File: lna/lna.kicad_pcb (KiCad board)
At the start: 2 copper layers, 40 x 20 mm, 1 part, among them U1 PGA-103+

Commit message: PCB part 1
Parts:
- added C1: 47pF, Capacitor_SMD:C_0603_1608Metric, F.Cu at (138.4, 103.0)
- added C2: 1.2pF, Capacitor_SMD:C_0603_1608Metric, F.Cu at (134.5, 95.0)
- added C3: 330pF, Capacitor_SMD:C_0603_1608Metric, F.Cu at (155.0, 99.0)
- added C4: 0.33uF, Capacitor_SMD:C_0603_1608Metric, F.Cu at (153.0, 89.5)
- added C5: 10uF, Capacitor_Tantalum_SMD:CP_EIA-3216-18_Kemet-A, F.Cu at (153.0, 87.0)
- added C6: 0.01uF, Capacitor_SMD:C_0603_1608Metric, F.Cu at (153.0, 95.0)
- added J1: Conn_Coaxial, Connector_Coaxial:SMA_Amphenol_132289_EdgeMount, F.Cu at (128.0, 95.0)
- added J2: V5-GND, Connector_PinHeader_2.54mm:PinHeader_1x02_P2.54mm_Vertical, F.Cu at (143.5, 87.0)
- added J3: Conn_Coaxial, Connector_Coaxial:SMA_Amphenol_132289_EdgeMount, F.Cu at (162.0, 95.0)
- added L1: 3nH, Inductor_SMD:L_0805_2012Metric, F.Cu at (138.4, 99.0)
- added L2: 120nH, Inductor_SMD:L_0805_2012Metric, F.Cu at (138.4, 95.0)
- added L3: 310nH, Inductor_SMD:L_0805_2012Metric, F.Cu at (142.9, 99.0)
- added L4: 310nH, Inductor_SMD:L_0805_2012Metric, F.Cu at (147.0, 99.0)
- added L5: 220nH, Inductor_SMD:L_0805_2012Metric, F.Cu at (153.0, 92.0)
- added R1: 150R, Resistor_SMD:R_0603_1608Metric, F.Cu at (151.0, 99.0)
- moved U1 1.70 mm to (145.0, 93.3), turned to 90 degrees
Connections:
- U1 pad 1: (no net) -> Net-(L2-Pad2)
- U1 pad 2: (no net) -> GND
- U1 pad 3: (no net) -> Net-(C6-Pad1)

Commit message: Routes
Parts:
- moved L2 0.06 mm to (138.5, 95.0), turned to 180 degrees
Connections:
- L2 pad 1: Net-(C2-Pad2) -> Net-(L3-Pad1)
- L2 pad 2: Net-(L2-Pad2) -> Net-(C2-Pad2)
- L3 pad 1: Net-(L2-Pad2) -> Net-(L3-Pad1)
- U1 pad 1: Net-(L2-Pad2) -> Net-(L3-Pad1)
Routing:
- net GND: track 0.00 -> 85.4 mm, vias 0 -> 4
- net Net-(C1-Pad1): track 0.00 -> 16.8 mm
- net 5V: track 0.00 -> 10.9 mm
- net Net-(C6-Pad1): track 0.00 -> 7.15 mm
- net Net-(C6-Pad2): track 0.00 -> 7.11 mm
- net Net-(L3-Pad1): track 0.00 -> 6.29 mm
- net Net-(C3-Pad1): track 0.00 -> 2.43 mm
- net Net-(L4-Pad2): track 0.00 -> 2.28 mm
- net Net-(L3-Pad2): track 0.00 -> 2.19 mm
- added copper zone on F.Cu, net GND
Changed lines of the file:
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@@
   (net 6 "Net-(C6-Pad2)")
   (net 7 "Net-(C6-Pad1)")
-  (net 8 "Net-(L2-Pad2)")
+  (net 8 "Net-(L3-Pad1)")
   (net 9 "Net-(L3-Pad2)")
   (net 10 "Net-(L4-Pad2)")
@@
     (fp_line (start 1.55 -2.25) (end 1.55 2.25) (layer "F.Fab") (width 0.1))
     (pad "1" smd rect (at -1.65 -1.5 90) (size 1.3 0.9) (layers "F.Cu" "F.Paste" "F.Mask")
-      (net 8 "Net-(L2-Pad2)"))
+      (net 8 "Net-(L3-Pad1)"))
     (pad "2" smd custom (at -1.5625 0 90) (size 1.475 0.9) (layers "F.Cu" "F.Paste" "F.Mask")
       (net 1 "GND") (pinfunction "GND") (zone_connect 2)
@@
   )
   (footprint "Inductor_SMD:L_0805_2012Metric" (layer "F.Cu")
-    (at 138.4375 95)
+    (at 138.5 95 180)
     (descr "Inductor SMD 0805 (2012 Metric), square (rectangular) end terminal, IPC_7351 nominal, (Body size source: https://docs.google.com/spreadsheets/d/1BsfQQcO9C6DZCsRaXUlFlo91Tg2WpOkGARC1WS5S8t0/edit?usp=sharing), generated with kicad-footprint-generator")
     (tags "inductor")
@@
     (property "Sheet name" "")
     (attr smd)
-    (fp_text reference "L2" (at 0 -1.65) (layer "F.SilkS")
+    (fp_text reference "L2" (at 0 1.5) (layer "F.SilkS")
       (effects (font (size 0.75 0.75) (thickness 0.15)))
     )
@@
     (fp_line (start 1 -0.6) (end 1 0.6) (layer "F.Fab") (width 0.1))
     (fp_line (start 1 0.6) (end -1 0.6) (layer "F.Fab") (width 0.1))
-    (pad "1" smd roundrect (at -0.9375 0) (size 0.975 1.4) (layers "F.Cu" "F.Paste" "F.Mask") (roundrect_rratio 0.25)
-      (net 3 "Net-(C2-Pad2)") (pinfunction "1"))
-    (pad "2" smd roundrect (at 0.9375 0) (size 0.975 1.4) (layers "F.Cu" "F.Paste" "F.Mask") (roundrect_rratio 0.25)
-      (net 8 "Net-(L2-Pad2)") (pinfunction "2"))
+    (pad "1" smd roundrect (at -0.9375 0 180) (size 0.975 1.4) (layers "F.Cu" "F.Paste" "F.Mask") (roundrect_rratio 0.25)
+      (net 8 "Net-(L3-Pad1)") (pinfunction "1"))
+    (pad "2" smd roundrect (at 0.9375 0 180) (size 0.975 1.4) (layers "F.Cu" "F.Paste" "F.Mask") (roundrect_rratio 0.25)
+      (net 3 "Net-(C2-Pad2)") (pinfunction "2"))
     (model "${KISYS3DMOD}/Inductor_SMD.3dshapes/L_0805_2012Metric.wrl"
       (offset (xyz 0 0 0))
@@
     (fp_line (start 1 0.6) (end -1 0.6) (layer "F.Fab") (width 0.1))
     (pad "1" smd roundrect (at -0.9375 0) (size 0.975 1.4) (layers "F.Cu" "F.Paste" "F.Mask") (roundrect_rratio 0.25)
-      (net 8 "Net-(L2-Pad2)") (pinfunction "1"))
+      (net 8 "Net-(L3-Pad1)") (pinfunction "1"))
     (pad "2" smd roundrect (at 0.9375 0) (size 0.975 1.4) (layers "F.Cu" "F.Paste" "F.Mask") (roundrect_rratio 0.25)
       (net 9 "Net-(L3-Pad2)") (pinfunction "2"))
@@
     (style (thickness 0.15) (arrow_length 1.27) (text_position_mode 0) (extension_height 0.58642) (extension_offset 0.5) keep_text_aligned)
   )
+  (segment (start 145 91.5) (end 145 94.8625) (width 1) (layer "F.Cu") (net 1))
+  (segment (start 162 99.25) (end 156.0375 99.25) (width 1) (layer "F.Cu") (net 1))
+  (segment (start 153.7875 89.5) (end 153.7875 87.5625) (width 1) (layer "F.Cu") (net 1))
+  (segment (start 162 90.75) (end 158.25 87) (width 1) (layer "F.Cu") (net 1))
+  (segment (start 156.0375 99.25) (end 155.7875 99) (width 1) (layer "F.Cu") (net 1))
+  (segment (start 128 90.75) (end 128 88.5) (width 1) (layer "F.Cu") (net 1))
+  (segment (start 162 90.75) (end 162 88.5) (width 1) (layer "F.Cu") (net 1))
+  (segment (start 143.5 90) (end 145 91.5) (width 1) (layer "F.Cu") (net 1))
+  (segment (start 139.375 99) (end 139.375 102.85) (width 1) (layer "F.Cu") (net 1))
+  (segment (start 143.5 87) (end 143.5 90) (width 1) (layer "F.Cu") (net 1))
+  (segment (start 128 101.5) (end 128 99.25) (width 1) (layer "F.Cu") (net 1))
+  (segment (start 153.7875 87.5625) (end 154.35 87) (width 1) (layer "F.Cu") (net 1))
+  (segment (start 162 99.25) (end 162 101.5) (width 1) (layer "F.Cu") (net 1))
+  (segment (start 158.25 87) (end 154.35 87) (width 1) (layer "F.Cu") (net 1))
+  (segment (start 139.375 102.85) (end 139.225 103) (width 1) (layer "F.Cu") (net 1))
+  (segment (start 162 101.5) (end 162 98) (width 1) (layer "F.Cu") (net 1))
+  (via (at 162 88.5) (size 0.8) (drill 0.4) (layers "F.Cu" "B.Cu") (net 1))
+  (via (at 128 101.5) (size 0.8) (drill 0.4) (layers "F.Cu" "B.Cu") (net 1))
+  (via (at 128 88.5) (size 0.8) (drill 0.4) (layers "F.Cu" "B.Cu") (net 1))
+  (via (at 162 101.5) (size 0.8) (drill 0.4) (layers "F.Cu" "B.Cu") (net 1))
+  (segment (start 128 88.5) (end 129.5 87) (width 1) (layer "B.Cu") (net 1))
+  (segment (start 128 101.5) (end 128 99.25) (width 1) (layer "B.Cu") (net 1))
+  (segment (start 162 99.25) (end 162 90.75) (width 1) (layer "B.Cu") (net 1))
+  (segment (start 162 90.75) (end 162 88.5) (width 1) (layer "B.Cu") (net 1))
+  (segment (start 128 90.75) (end 128 88.5) (width 1) (layer "B.Cu") (net 1))
+  (segment (start 131.75 87) (end 143.5 87) (width 1) (layer "B.Cu") (net 1))
+  (segment (start 128 99.25) (end 128 90.75) (width 1) (layer "B.Cu") (net 1))
+  (segment (start 129.5 87) (end 131.75 87) (width 1) (layer "B.Cu") (net 1))
+  (segment (start 162 99.25) (end 162 101.5) (width 1) (layer "B.Cu") (net 1))
+  (segment (start 133 95) (end 128 95) (width 3) (layer "F.Cu") (net 2))
+  (segment (start 133.75 95) (end 133.75 97.75) (width 1) (layer "F.Cu") (net 2))
+  (segment (start 137.65 99.15) (end 137.5 99) (width 1) (layer "F.Cu") (net 2))
+  (segment (start 137.65 103) (end 137.65 99.15) (width 1) (layer "F.Cu") (net 2))
+  (segment (start 135 99) (end 137.5 99) (width 1) (layer "F.Cu") (net 2))
+  (segment (start 133.75 97.75) (end 135 99) (width 1) (layer "F.Cu") (net 2))
+  (segment (start 133.75 95) (end 133 95) (width 1) (layer "F.Cu") (net 2))
+  (segment (start 136.325 95) (end 136.8 95) (width 3) (layer "F.Cu") (net 3))
+  (segment (start 154.2125 99) (end 151.7875 99) (width 1) (layer "F.Cu") (net 4))
+  (segment (start 151.65 88.9375) (end 152.2125 89.5) (width 1) (layer "F.Cu") (net 5))
+  (segment (start 152.2125 91.85) (end 152.0625 92) (width 1) (layer "F.Cu") (net 5))
+  (segment (start 151.65 87) (end 151.65 88.9375) (width 1) (layer "F.Cu") (net 5))
+  (segment (start 146.04 87) (end 151.65 87) (width 1) (layer "F.Cu") (net 5))
+  (segment (start 152.2125 89.5) (end 152.2125 91.85) (width 1) (layer "F.Cu") (net 5))
+  (segment (start 154.8875 95) (end 162 95) (width 3) (layer "F.Cu") (net 6))
+  (segment (start 152.1625 94.95) (end 152.2125 95) (width 1) (layer "F.Cu") (net 7))
+  (segment (start 147.8 94.95) (end 151.1625 94.95) (width 3) (layer "F.Cu") (net 7))
+  (segment (start 153.9375 92) (end 153.9375 92.7) (width 1) (layer "F.Cu") (net 7))
+  (segment (start 152.2125 94.425) (end 153.9375 92.7) (width 1) (layer "F.Cu") (net 7))
+  (segment (start 152.2125 94.425) (end 152.2125 95) (width 1) (layer "F.Cu") (net 7))
+  (segment (start 141.5 95) (end 141.5 97.5) (width 1) (layer "F.Cu") (net 8))
+  (segment (start 141.5 98.5) (end 142 99) (width 1) (layer "F.Cu") (net 8))
+  (segment (start 141.5 97.5) (end 141.5 98.5) (width 1) (layer "F.Cu") (net 8))
+  (segment (start 143.45 95) (end 143.5 94.95) (width 1) (layer "F.Cu") (net 8))
+  (segment (start 140.4375 95) (end 142.45 95) (width 3) (layer "F.Cu") (net 8))
+  (segment (start 146.0625 99) (end 143.875 99) (width 1) (layer "F.Cu") (net 9))
+  (segment (start 150.2125 99) (end 147.9375 99) (width 1) (layer "F.Cu") (net 10))
+  (zone (net 1) (net_name "GND") (layer "F.Cu") (hatch edge 0.508)
+    (connect_pads (clearance 0.508))
+    (min_thickness 0.254) (filled_areas_thickness no)
+    (fill yes (thermal_gap 0.508) (thermal_bridge_width 0.508))
+    (polygon
+      (pts
+        (xy 165 105)
+        (xy 125 105)
+        (xy 125 85)
+        (xy 165 85)
+      )
+    )
+  )
 )

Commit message: Final v1
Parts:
- added FB1: 600R/0.5A, fbead:Murata-BLM18-0.15-t0.8-0-0-IPC_A, F.Cu at (150.0, 87.8)
- moved C3 5.94 mm to (149.2, 100.2)
- moved C1 5.60 mm to (133.6, 100.2)
- moved R1 5.34 mm to (145.8, 100.2)
- moved L1 4.97 mm to (133.6, 97.9)
- moved L4 4.95 mm to (142.2, 100.2)
- moved L3 2.37 mm to (141.4, 97.2), turned to -90 degrees
- moved C5 1.79 mm to (154.6, 87.8)
- moved C4 1.12 mm to (154.0, 90.0)
- moved L5 0.76 mm to (152.3, 92.2), turned to 0 degrees
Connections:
- C4 pad 1: 5V -> Net-(C4-Pad1)
- C5 pad 1: 5V -> Net-(C4-Pad1)
- L5 pad 2: 5V -> Net-(C4-Pad1)
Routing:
- net GND: track 85.4 -> 33.8 mm, vias 4 -> 6
- net 5V: track 10.9 -> 3.52 mm
- net Net-(C4-Pad1): track 0.00 -> 6.89 mm
- net Net-(C1-Pad1): track 16.8 -> 11.2 mm
- net Net-(L2-Pad1): track 6.29 -> 2.08 mm
- net Net-(C3-Pad1): track 2.43 -> 1.81 mm
- added copper zone on B.Cu, net GND

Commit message: Add some fixes
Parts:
- added C7: 100pF, Capacitor_SMD:C_0603_1608Metric, F.Cu at (153.0, 95.0)
- added G***: LOGO, lna_images:name, F.Cu at (130.8, 103.8)
- C4: value 0.33uF -> 100pF
- C5: value 10uF -> 100nF; footprint Capacitor_Tantalum_SMD:CP_EIA-3216-18_Kemet-A -> Capacitor_SMD:C_0603_1608Metric
- C6: value 0.01uF -> 10uF; footprint Capacitor_SMD:C_0603_1608Metric -> Capacitor_Tantalum_SMD:CP_EIA-3216-18_Kemet-A
- moved C6 8.66 mm to (155.8, 86.8)
- moved C1 7.66 mm to (132.6, 92.6), turned to 90 degrees
- moved C5 1.20 mm to (154.7, 89.0)
- moved L5 1.06 mm to (151.2, 92.2)
- moved C4 1.05 mm to (154.7, 90.8), turned to 180 degrees
- moved L1 1.04 mm to (132.6, 97.6), turned to -90 degrees
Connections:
- C4 pad 1: Net-(C4-Pad1) -> GND
- C4 pad 2: GND -> Net-(C4-Pad2)
- C5 pad 1: Net-(C4-Pad1) -> Net-(C4-Pad2)
- C6 pad 1: Net-(C6-Pad1) -> Net-(C4-Pad2)
- C6 pad 2: Net-(C6-Pad2) -> GND
- FB1 pad 2: Net-(C4-Pad1) -> Net-(C4-Pad2)
- J3 pad 1: Net-(C6-Pad2) -> Net-(C7-Pad2)
- L5 pad 1: Net-(C6-Pad1) -> Net-(C7-Pad1)
- L5 pad 2: Net-(C4-Pad1) -> Net-(C4-Pad2)
- U1 pad 3: Net-(C6-Pad1) -> Net-(C7-Pad1)
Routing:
- net Net-(C4-Pad2): track 0.00 -> 9.92 mm
- net Net-(C7-Pad1): track 0.00 -> 7.91 mm
- net Net-(C6-Pad1): track 7.54 -> 0.00 mm
- net Net-(C7-Pad2): track 0.00 -> 7.11 mm
- net Net-(C6-Pad2): track 7.11 -> 0.00 mm
- net Net-(C4-Pad1): track 6.89 -> 0.00 mm
- net Net-(C1-Pad1): track 11.2 -> 6.24 mm
- net GND: track 33.8 -> 32.7 mm, vias 6 -> 7

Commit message: Refill zones
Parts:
- moved G*** 3.26 mm to (134.0, 103.2)
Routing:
- net GND: vias 7 -> 8

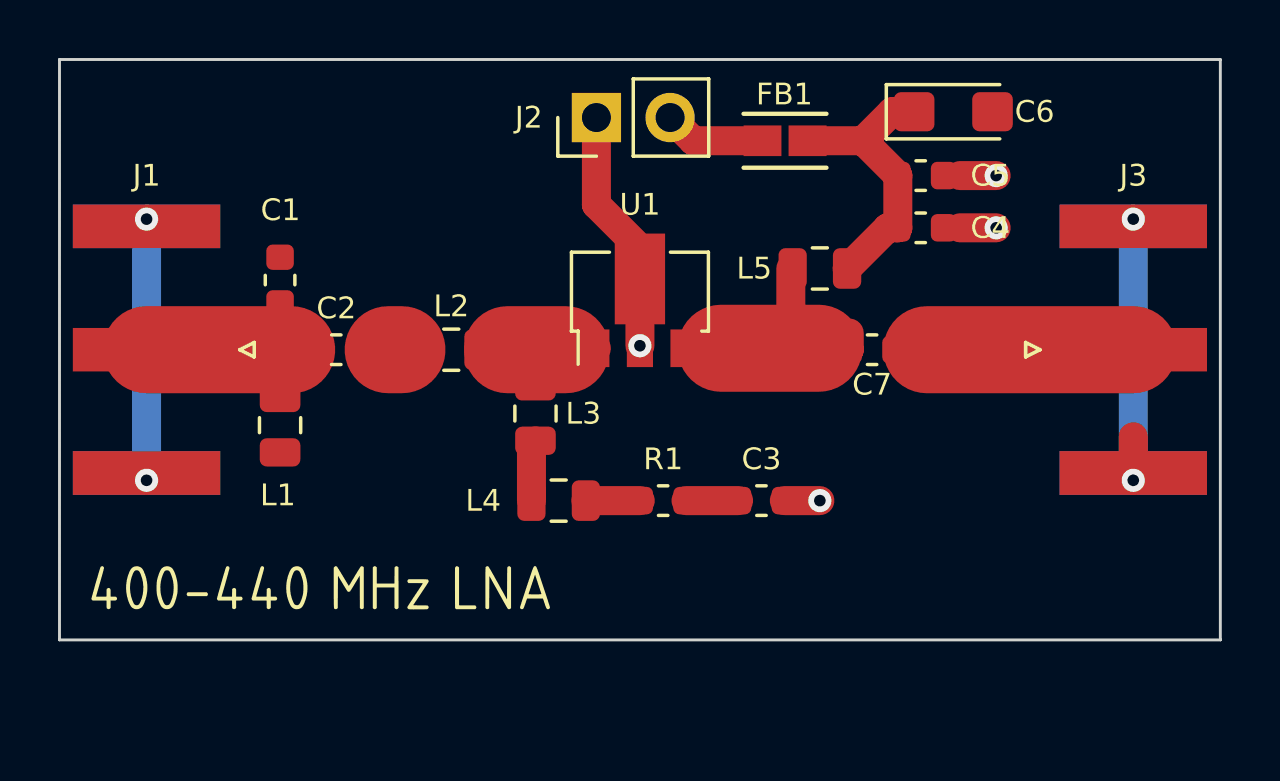
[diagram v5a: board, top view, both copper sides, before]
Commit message: Solid zones
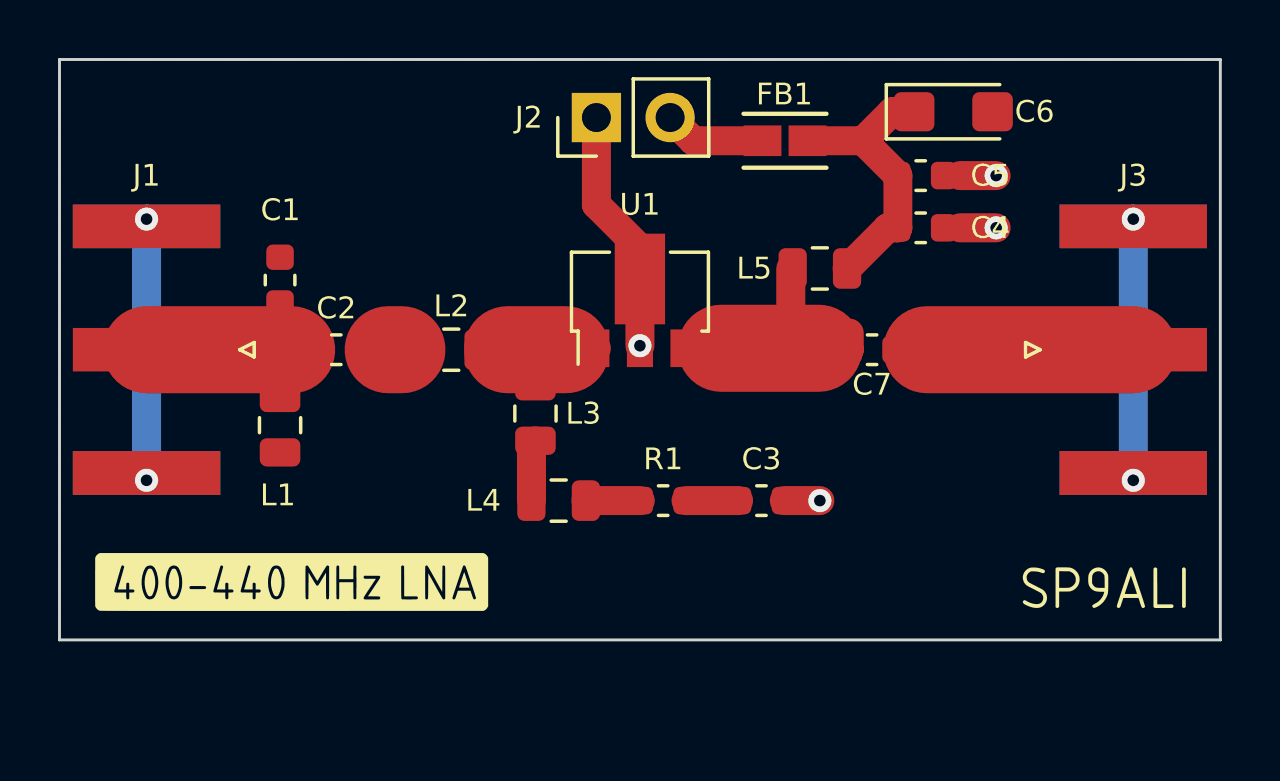
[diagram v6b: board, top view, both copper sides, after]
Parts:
- added G***: LOGO, lna_images:sign, F.Cu at (161.0, 103.2)
- moved G*** 1.02 mm to (133.0, 103.0)
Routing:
- net GND: track 32.7 -> 31.2 mm

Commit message: Images
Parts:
- removed the G*** at (133.0, 103.0)
- added G***: LOGO, lna_images:name, F.Cu at (134.0, 103.0)
- added G***: LOGO, lna_images:name, F.Cu at (131.8, 106.2)
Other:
- board text added: "5V"
- board text added: "G"
- board text added: "IN"
- board text added: "OUT"

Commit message: LNA images
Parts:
- removed the G*** at (134.0, 103.0)
- removed the G*** at (131.8, 106.2)
- added G***: LOGO, lna_images:LNA, F.Cu at (136.5, 103.0)
- added G***: LOGO, lna_images:name, F.Cu at (136.2, 87.5)
- added G***: LOGO, lna_images:BACKGROUND, B.Cu at (145.2, 95.0)
- moved G*** 0.32 mm to (160.8, 103.0)
